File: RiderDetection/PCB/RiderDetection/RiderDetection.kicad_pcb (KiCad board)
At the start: 2 copper layers, 87.6 x 69.8 mm, 21 parts, among them J1 Conn_01x19, J2 Conn_01x19, J3 Conn_01x06, J4 Conn_01x03_Male, J5 Conn_01x03_Male, K1 G5V-1, K2 G5V-1, K3 G5V-1, U1 ULN2003A, U2 TSR_1-2450

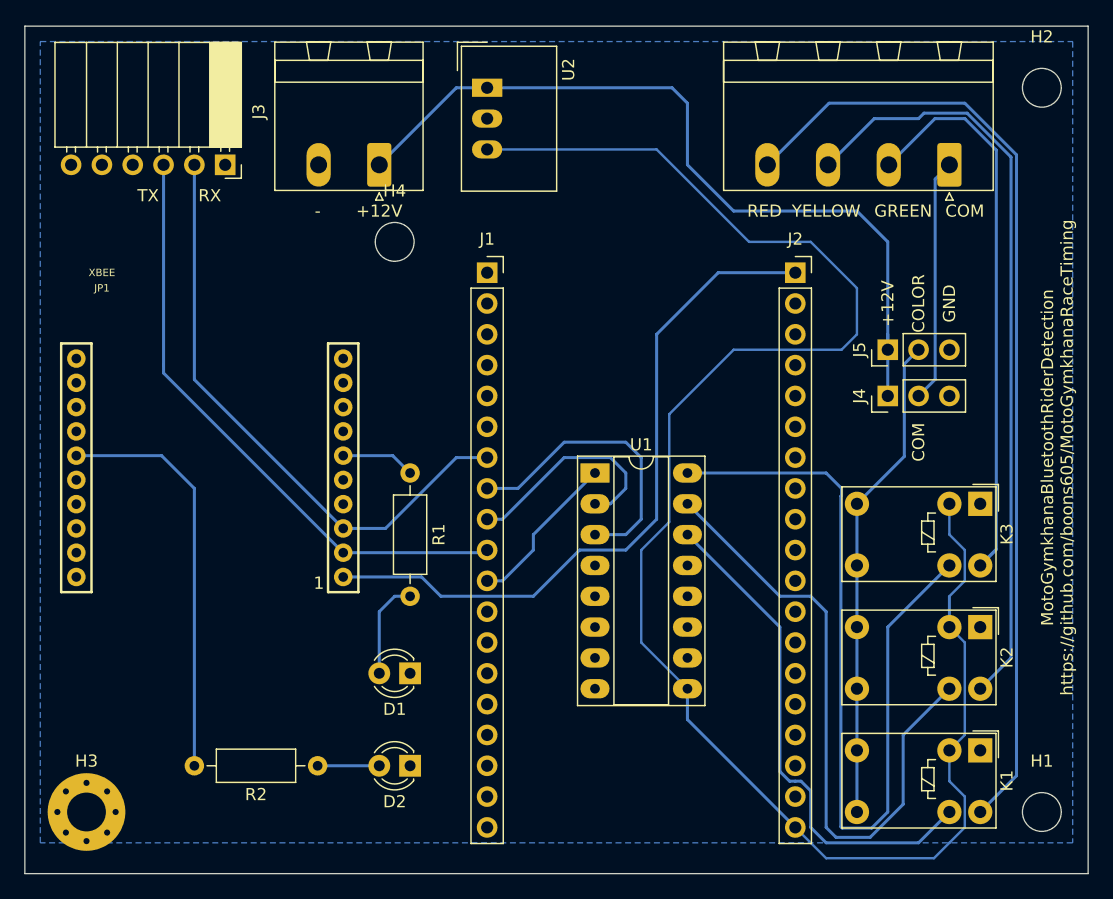
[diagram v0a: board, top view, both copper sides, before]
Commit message: Issue 19: Carrier PCB for rider ID, V2 with corrections
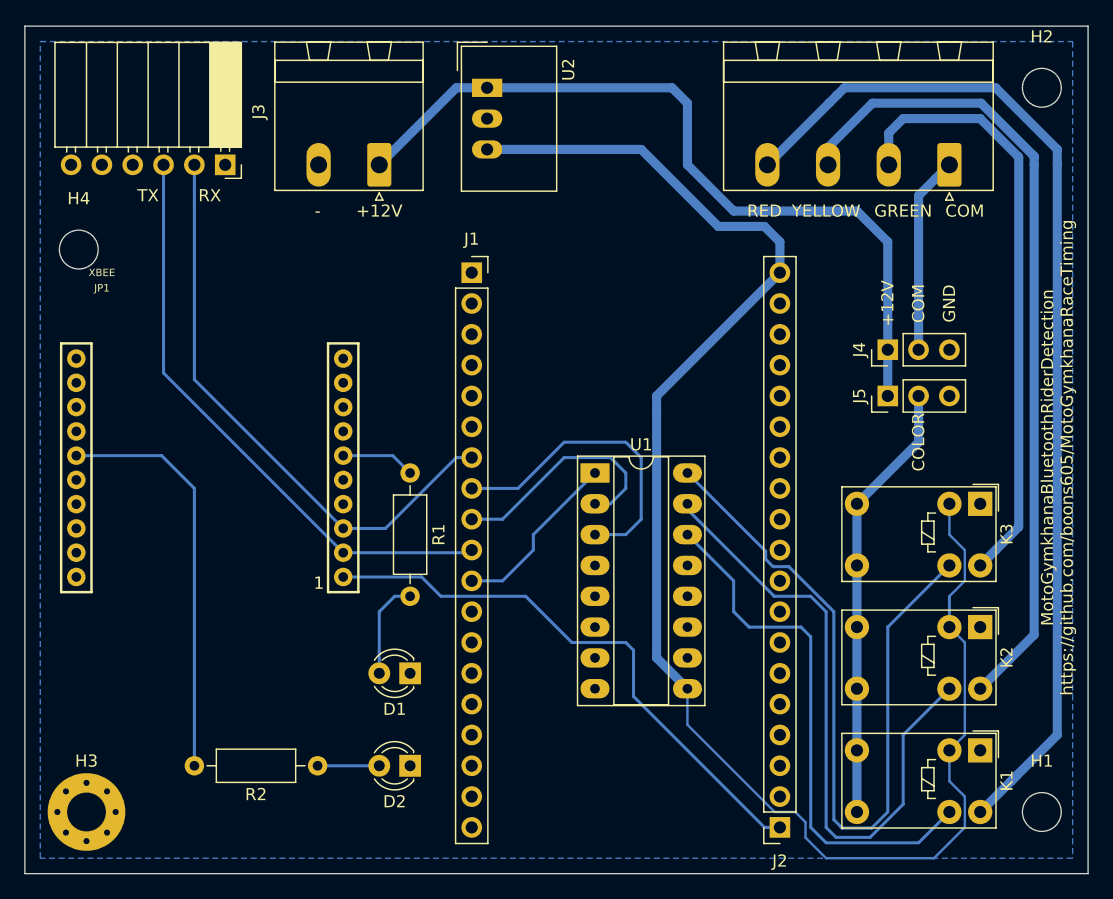
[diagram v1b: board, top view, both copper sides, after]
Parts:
- moved J2 45.7 mm to (111.8, 114.3), turned to 180 degrees
- moved H4 26.0 mm to (54.0, 66.7)
- moved J4 3.81 mm to (120.7, 74.9)
- moved J5 3.81 mm to (120.7, 78.7)
- moved J1 1.27 mm to (86.4, 68.6)
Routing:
- net +5V: track 142.9 -> 130.9 mm
- net +3V3: track 57.9 -> 46.9 mm
- net COL_RD: track 79.8 -> 86.5 mm
- net Net-(K3-Pad9): track 68.0 -> 62.2 mm
- net COL_YW: track 63.2 -> 67.5 mm
- net START_COLOR_COM: track 40.2 -> 36.4 mm
- net START_COM: track 20.1 -> 16.3 mm
- net COL_GRN: track 48.1 -> 50.8 mm
- net Net-(K1-Pad9): track 41.9 -> 43.9 mm
- net +12V: track 66.7 -> 65.5 mm
- net RXD: track 49.7 -> 48.5 mm
- net Net-(J1-Pad9): track 18.4 -> 19.7 mm
- net Net-(J1-Pad8): track 24.2 -> 25.5 mm
- net Net-(J1-Pad11): track 13.3 -> 14.6 mm
- net TXD: track 50.1 -> 48.8 mm
